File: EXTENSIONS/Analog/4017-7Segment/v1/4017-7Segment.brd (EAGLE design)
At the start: 38 x 25 mm, 8 parts

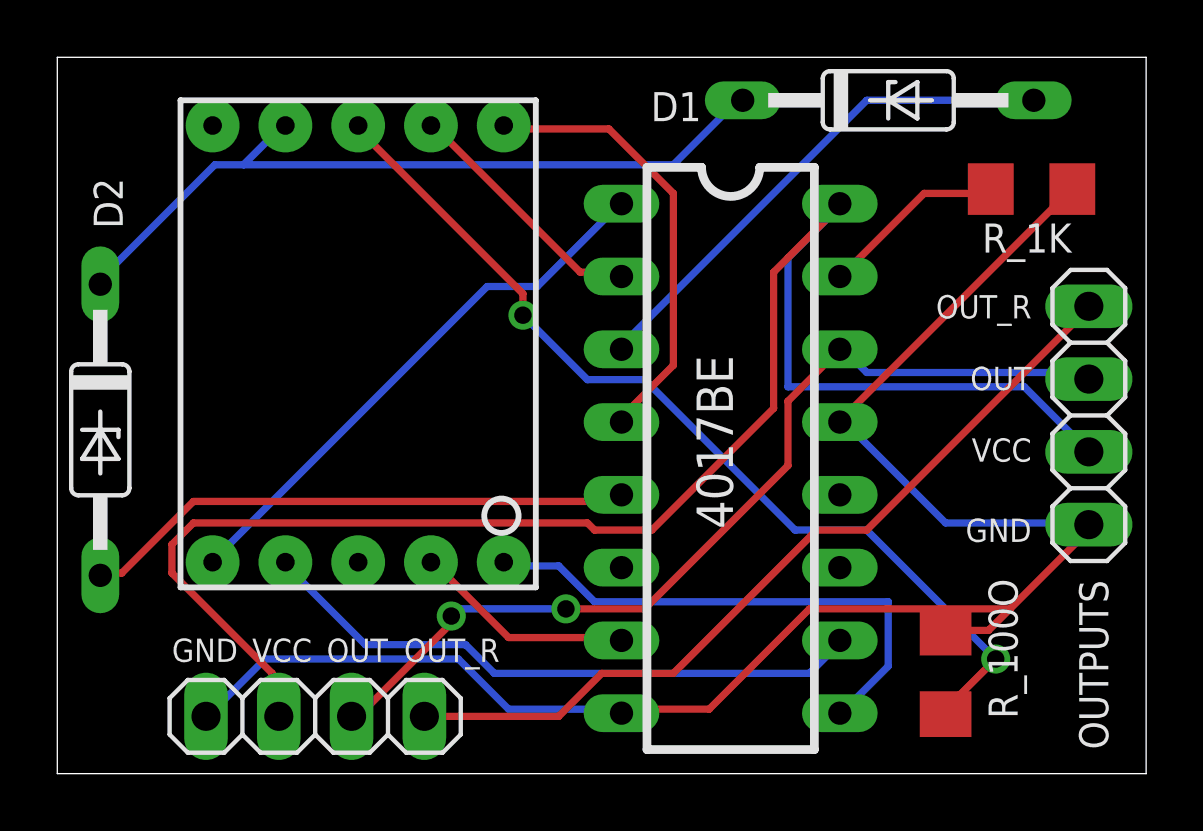
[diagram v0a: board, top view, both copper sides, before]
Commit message: board 4017-7Segment v2 on hold, until I received chip 4017B
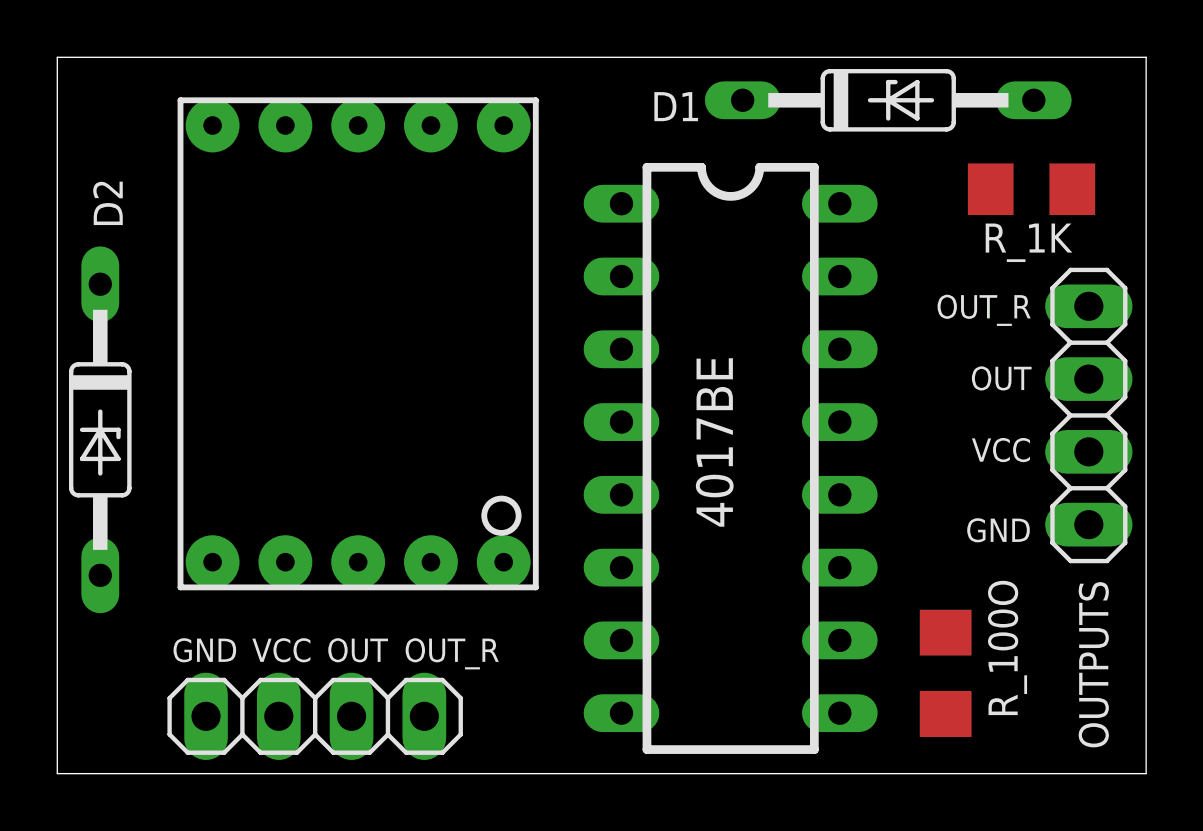
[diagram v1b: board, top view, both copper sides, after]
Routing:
- net GND: track 59.6 -> 0.00 mm
- net VCC: track 57.5 -> 0.00 mm
- net N$2: track 33.1 -> 0.00 mm, vias 2 -> 0
- net TMR555_OUTPUT: track 33.1 -> 0.00 mm, vias 2 -> 0
- net TMR555_OUTPUT_REVERSE: track 29.2 -> 0.00 mm
- net SEG_F: track 27.2 -> 0.00 mm
- net SEG_D: track 21.5 -> 0.00 mm
- net SEG_E: track 19.5 -> 0.00 mm
- net N$4: track 19.4 -> 0.00 mm
- net SEG_DP: track 18.6 -> 0.00 mm
- net N$3: track 18.1 -> 0.00 mm
- net SEG_B: track 15.6 -> 0.00 mm
- net SEG_A: track 8.81 -> 0.00 mm
- net SEG_C: track 7.75 -> 0.00 mm
- net N$1: track 6.55 -> 0.00 mm
